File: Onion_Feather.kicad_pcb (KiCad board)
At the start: 2 copper layers, 59.7 x 53.3 mm, 19 parts, among them J1 HR911105A, J2 CON_HEADER_PRG_AVR_ICSP-PTH, J3 Conn_01x02, J4 USB_A, P1 PADNORMAL, P2 PADNORMAL, U1 ONION-OMEGA2, U2 CJ1117 3V3, U3 CP2102N-A01-GQFN24

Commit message: More wiring
Signed-off-by: Tisham Dhar <whatnickd@gmail.com>
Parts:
- removed FTDI1: CON_HEADER_1X06-PTH, Connector_PinHeader_2.54mm:PinHeader_1x06_P2.54mm_Horizontal
- removed PTH1: CON_HEADER_1X06, Connector_PinHeader_2.54mm:PinHeader_1x06_P2.54mm_Horizontal
- JP1: moved to B.Cu
- R1, R2: footprint Resistor_SMD:R_0805_2012Metric -> Resistor_SMD:R_0603_1608Metric
- U2: value CJ1117 3V3 -> AP1117-33; footprint Package_TO_SOT_SMD:SOT-89-3 -> Package_TO_SOT_SMD:SOT-223-3_TabPin2
- moved JP1 57.5 mm to (139.7, 78.7)
- moved R2 49.0 mm to (156.8, 93.5), turned to 270 degrees
- moved P1 41.5 mm to (152.4, 99.1)
- moved P2 37.7 mm to (155.6, 99.1)
- moved R1 33.7 mm to (154.9, 93.5), turned to 270 degrees
- moved U3 2.84 mm to (138.4, 71.8)
- moved C1 2.22 mm to (135.9, 79.0)
- moved U2 1.80 mm to (130.2, 76.2)
- renumbered I2C1 to J5
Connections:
- net Net-(J4-Pad1) renamed 5V_BOOST
- net Net-(U1-Pad21) renamed /OnionModule/ETH_RX+
- net Net-(U1-Pad22) renamed /OnionModule/ETH_RX-
- net Net-(U1-Pad23) renamed /OnionModule/ETH_TX+
- net Net-(U1-Pad24) renamed /OnionModule/ETH_TX-
- J2 pad 1: /OnionModule/MISO -> MISO
- J2 pad 3: /OnionModule/CLK -> SCLK
- J2 pad 4: /OnionModule/MOSI -> MOSI
- J2 pad 5: /OnionModule/CS -> CS
- J4 pad 2: Net-(J4-Pad2) -> USB_OUT-
- J4 pad 3: Net-(J4-Pad3) -> USB_OUT+
- J5 pad 3: /OnionModule/SCL -> SCL
- J5 pad 4: /OnionModule/SDA -> SDA
- JP1 pad 2: /OnionModule/FT_PWR -> /OnionModule/FTDI_PWR
- MS1 pad 11: Net-(MS1-Pad11) -> SCLK
- MS1 pad 12: Net-(MS1-Pad12) -> MOSI
- MS1 pad 13: Net-(MS1-Pad13) -> MISO
- MS1 pad 17: Net-(MS1-Pad17) -> SDA
- MS1 pad 18: Net-(MS1-Pad18) -> SCL
- MS1 pad 22: Net-(MS1-Pad22) -> CS
- R1 pad 1: /OnionModule/SDA -> SDA
- R2 pad 1: /OnionModule/SCL -> SCL
- U1 pad 10: /OnionModule/MISO -> MISO
- U1 pad 11: /OnionModule/MOSI -> MOSI
- U1 pad 12: /OnionModule/CLK -> SCLK
- U1 pad 13: /OnionModule/CS -> CS
- U1 pad 17: /OnionModule/SDA -> SDA
- U1 pad 18: /OnionModule/SCL -> SCL
- U1 pad 27: /OnionModule/TX -> /OnionModule/FTDI_RXD
- U1 pad 28: /OnionModule/RX -> /OnionModule/FTDI_TXD
- U1 pad 29: Net-(U1-Pad29) -> USB_OUT-
- U1 pad 30: Net-(U1-Pad30) -> USB_OUT+

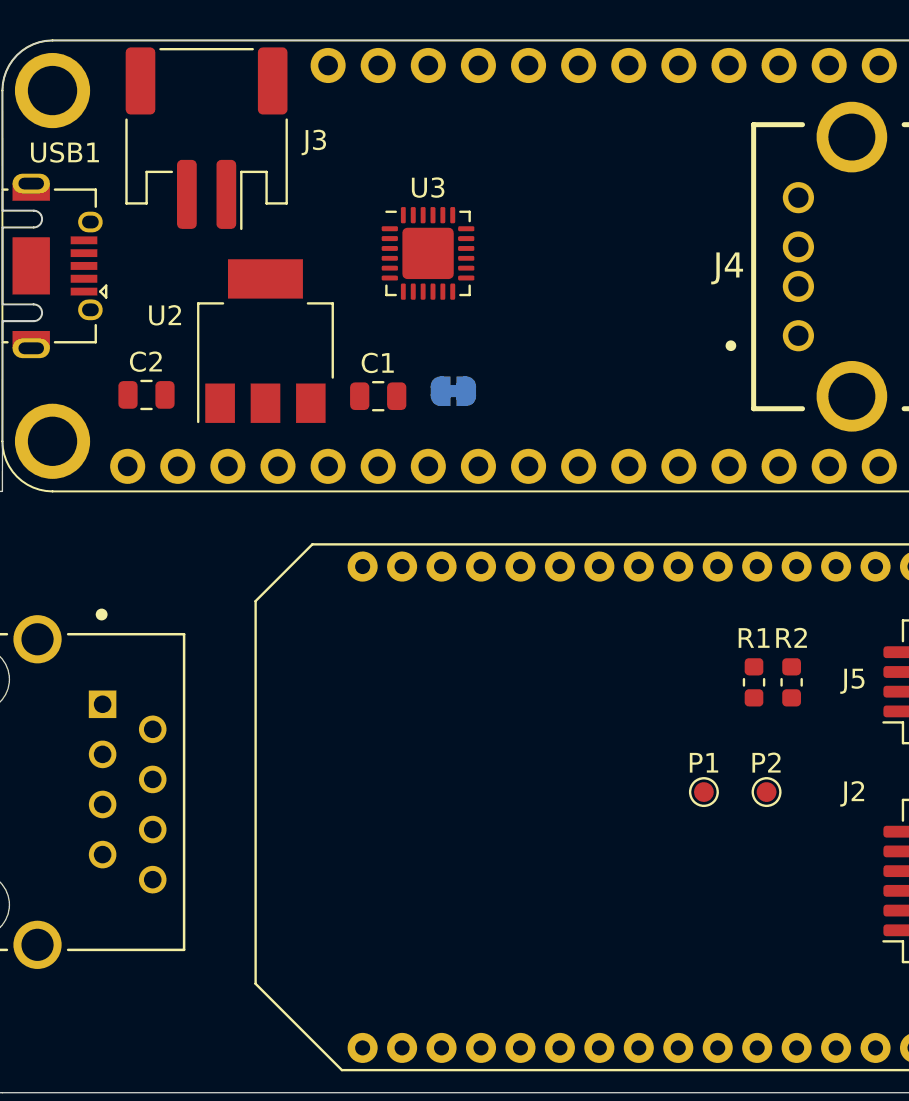
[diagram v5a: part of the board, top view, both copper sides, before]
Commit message: Get fancy with the battery
Signed-off-by: Tisham Dhar <whatnickd@gmail.com>
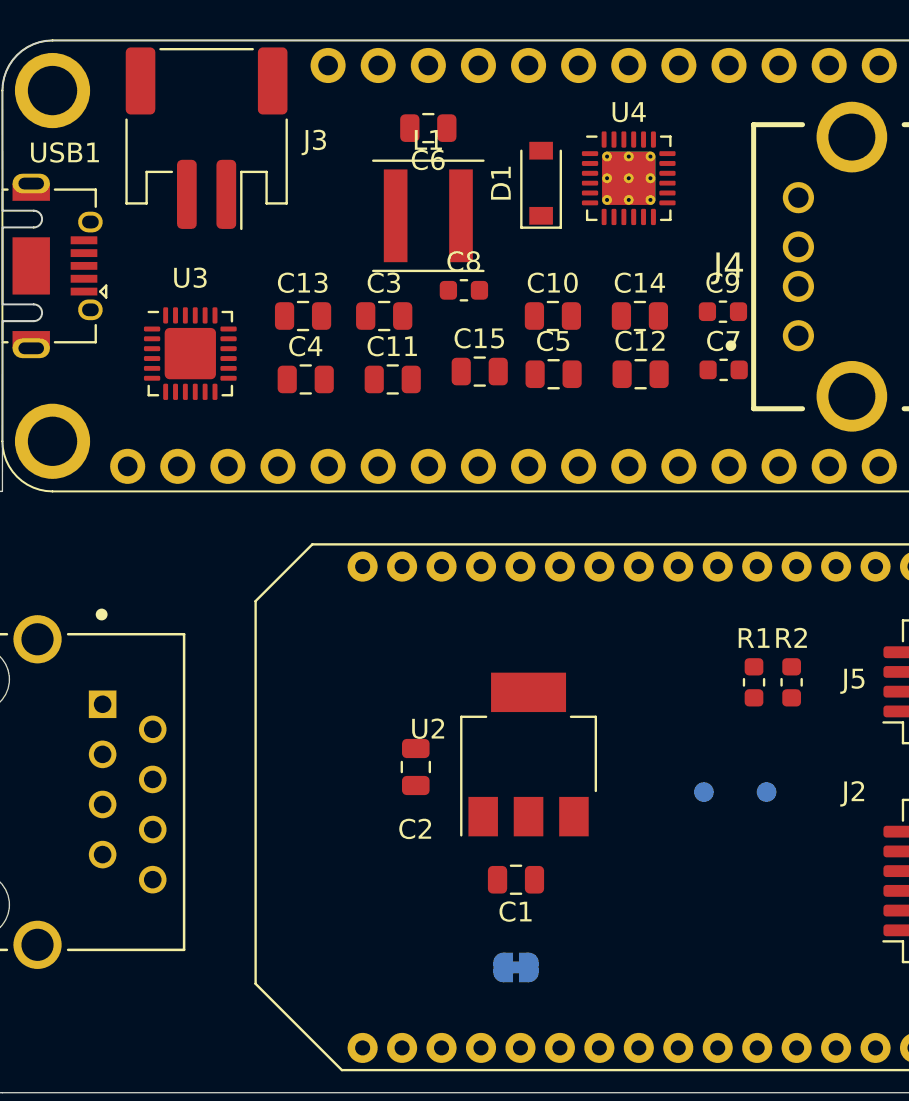
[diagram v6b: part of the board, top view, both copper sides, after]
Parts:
- added C10: 10u, Capacitor_SMD:C_0805_2012Metric, F.Cu at (144.7, 74.9)
- added C11: 10u, Capacitor_SMD:C_0805_2012Metric, F.Cu at (136.6, 78.1)
- added C12: 10u, Capacitor_SMD:C_0805_2012Metric, F.Cu at (149.2, 77.9)
- added C13: 47u, Capacitor_SMD:C_0805_2012Metric, F.Cu at (132.1, 74.9)
- added C14: 10u, Capacitor_SMD:C_0805_2012Metric, F.Cu at (149.2, 74.9)
- added C15: 10u, Capacitor_SMD:C_0805_2012Metric, F.Cu at (141.0, 77.7)
- added C3: 10u, Capacitor_SMD:C_0805_2012Metric, F.Cu at (136.2, 74.9)
- added C4: 10u, Capacitor_SMD:C_0805_2012Metric, F.Cu at (132.2, 78.1)
- added C5: 10u, Capacitor_SMD:C_0805_2012Metric, F.Cu at (144.8, 77.9)
- added C6: 4.7u, Capacitor_SMD:C_0805_2012Metric, F.Cu at (138.4, 65.4)
- added C7: 47n, Capacitor_SMD:C_0603_1608Metric, F.Cu at (153.4, 77.7)
- added C8: 100n, Capacitor_SMD:C_0603_1608Metric, F.Cu at (140.2, 73.6)
- added C9: 1u, Capacitor_SMD:C_0603_1608Metric, F.Cu at (153.4, 74.7)
- added D1: D_Schottky, Diode_SMD:D_SOD-123, F.Cu at (144.1, 68.2)
- added L1: 2.2u, Inductor_SMD:L_Coilcraft_XAL5030, F.Cu at (138.4, 69.8)
- added U4: BQ25895RTW, Package_DFN_QFN:Texas_S-PWQFN-N24_EP2.7x2.7mm_ThermalVias, F.Cu at (148.6, 67.9)
- C1, C2: value 10uF -> 10u
- P1, P2: moved to B.Cu
- moved JP1 29.4 mm to (142.9, 108.0)
- moved C1 25.5 mm to (142.9, 103.5), turned to 180 degrees
- moved U2 24.8 mm to (143.5, 97.2)
- moved C2 23.3 mm to (137.8, 97.8), turned to 270 degrees
- moved U3 13.1 mm to (126.4, 76.8)
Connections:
- net Net-(USB1-Pad4) renamed /Power Subsystems/ID
- J3 pad 1: Net-(J3-Pad1) -> GND
- USB1 pad 2: GND -> /Power Subsystems/USB_IN-
- USB1 pad 3: Net-(USB1-Pad3) -> /Power Subsystems/USB_IN+

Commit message: Work on Power and USB-Serial
Signed-off-by: Tisham Dhar <whatnickd@gmail.com>
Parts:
- added C16: 1u, Capacitor_SMD:C_0603_1608Metric, F.Cu at (124.5, 73.0)
- added C17: 100n, Capacitor_SMD:C_0603_1608Metric, F.Cu at (128.5, 73.0)
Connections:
- net Net-(C12-Pad2) renamed /Power Subsystems/VBAT
- net Net-(U3-Pad19) renamed /USB Interfaces/RTS
- net Net-(U3-Pad20) renamed USB_TX
- net Net-(U3-Pad21) renamed USB_RX
- net Net-(U3-Pad23) renamed /USB Interfaces/DTR
- net Net-(U3-Pad3) renamed /USB Interfaces/USB_IN+
- net Net-(U3-Pad4) renamed /USB Interfaces/USB_IN-
- net Net-(U4-Pad24) renamed /Power Subsystems/DSEL
- C10 pad 2: /Power Subsystems/PMID -> 5V_BOOST
- C13 pad 2: /Power Subsystems/PMID -> 5V_BOOST
- C8 pad 2: /Power Subsystems/PMID -> 5V_BOOST
- C9 pad 2: /Power Subsystems/PMID -> 5V_BOOST
- D1 pad 1: /Power Subsystems/PMID -> 5V_BOOST
- J4 pad 4: Net-(J4-Pad4) -> GND
- J4 pad 5: Net-(J4-Pad5) -> GND
- U3 pad 2: Net-(U3-Pad2) -> GND
- U3 pad 25: Net-(U3-Pad25) -> GND
- U3 pad 5: Net-(U3-Pad5) -> 3.3V
- U3 pad 6: Net-(U3-Pad6) -> 3.3V
- U3 pad 7: Net-(U3-Pad7) -> VIN
- U3 pad 8: Net-(U3-Pad8) -> VIN
- U4 pad 23: /Power Subsystems/PMID -> 5V_BOOST

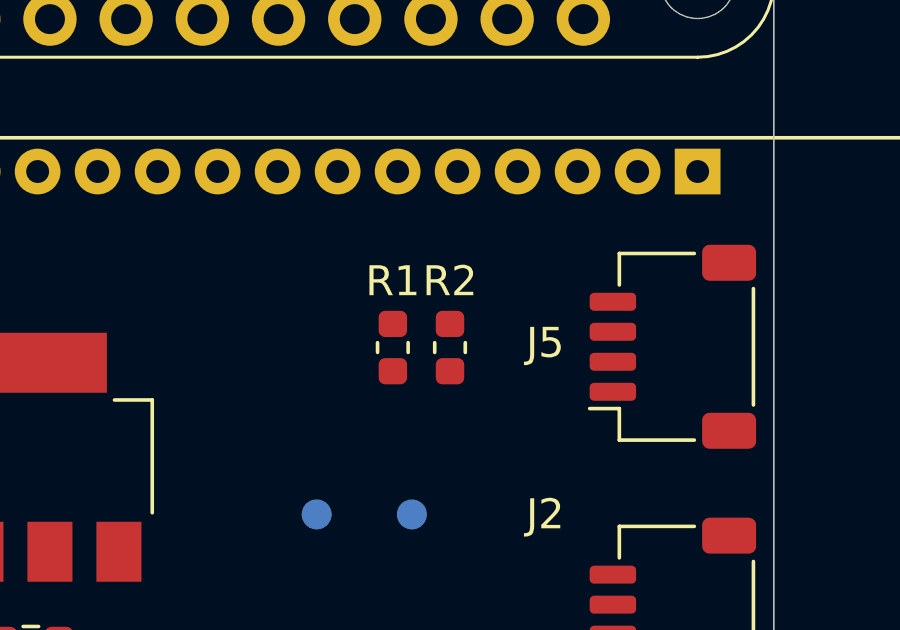
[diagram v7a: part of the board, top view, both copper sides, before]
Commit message: Swap pins to use Qwiic spec
Signed-off-by: Tisham Dhar <whatnickd@gmail.com>
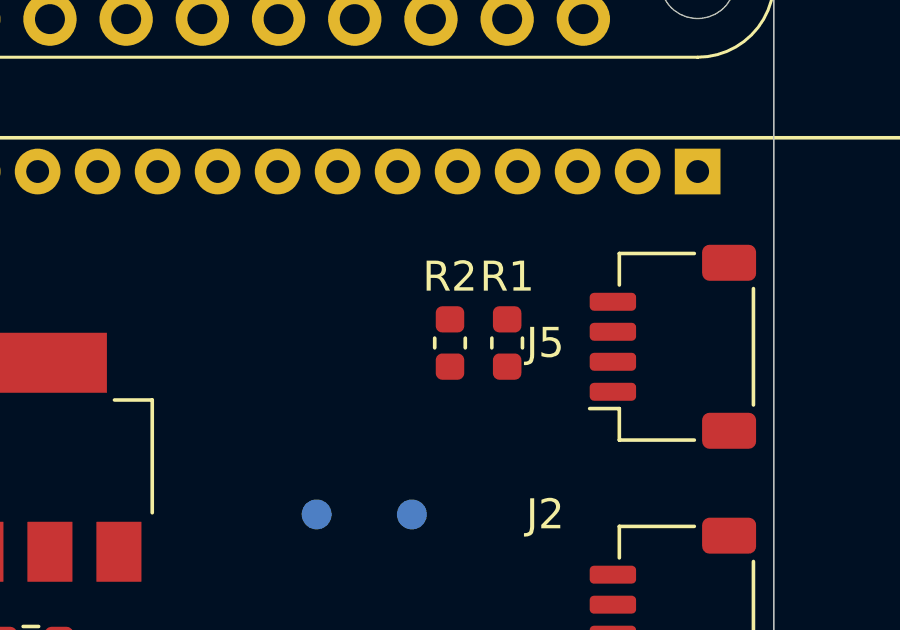
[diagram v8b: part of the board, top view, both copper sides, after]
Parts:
- moved R1 3.81 mm to (158.8, 93.3)
- moved R2 0.15 mm to (156.8, 93.3)
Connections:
- J5 pad 1: 3.3V -> GND
- J5 pad 2: GND -> 3.3V
- J5 pad 3: SCL -> SDA
- J5 pad 4: SDA -> SCL
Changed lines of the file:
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@@
     (47 F.CrtYd user)
     (48 B.Fab user)
-    (49 F.Fab user)
+    (49 F.Fab user hide)
   )
   (setup
@@
   )
   (module Resistor_SMD:R_0603_1608Metric (layer F.Cu)
-    (at 156.845 93.4975 270)
+    (at 156.845 93.345 270)
     (descr "Resistor SMD 0603 (1608 Metric), square (rectangular) end terminal, IPC_7351 nominal, (Body size source: http://www.tortai-tech.com/upload/download/2011102023233369053.pdf), generated with kicad-footprint-generator")
     (tags resistor)
@@
   )
   (module Resistor_SMD:R_0603_1608Metric (layer F.Cu)
-    (at 154.94 93.4975 270)
+    (at 158.75 93.345 270)
     (descr "Resistor SMD 0603 (1608 Metric), square (rectangular) end terminal, IPC_7351 nominal, (Body size source: http://www.tortai-tech.com/upload/download/2011102023233369053.pdf), generated with kicad-footprint-generator")
     (tags resistor)
@@
     (pad MP smd roundrect (at -2.8 1.875 90) (size 1.2 1.8) (layers F.Cu F.Paste F.Mask) (roundrect_rratio 0.208333))
     (pad 4 smd roundrect (at 1.5 -2 90) (size 0.6 1.55) (layers F.Cu F.Paste F.Mask) (roundrect_rratio 0.25)
+      (net 78 SCL))
+    (pad 3 smd roundrect (at 0.5 -2 90) (size 0.6 1.55) (layers F.Cu F.Paste F.Mask) (roundrect_rratio 0.25)
       (net 77 SDA))
-    (pad 3 smd roundrect (at 0.5 -2 90) (size 0.6 1.55) (layers F.Cu F.Paste F.Mask) (roundrect_rratio 0.25)
-      (net 78 SCL))
     (pad 2 smd roundrect (at -0.5 -2 90) (size 0.6 1.55) (layers F.Cu F.Paste F.Mask) (roundrect_rratio 0.25)
-      (net 35 GND))
+      (net 37 3.3V))
     (pad 1 smd roundrect (at -1.5 -2 90) (size 0.6 1.55) (layers F.Cu F.Paste F.Mask) (roundrect_rratio 0.25)
-      (net 37 3.3V))
+      (net 35 GND))
     (model ${KISYS3DMOD}/Connector_JST.3dshapes/JST_SH_SM04B-SRSS-TB_1x04-1MP_P1.00mm_Horizontal.wrl
       (at (xyz 0 0 0))
